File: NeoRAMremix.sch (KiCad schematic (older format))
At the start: 16 parts, among them P1 C64-Exp-Port, Q1 2N3904, U1 HM628512BFP-5, U2 HM628512BFP-5, U3 HM628512BFP-5, U4 HM628512BFP-5

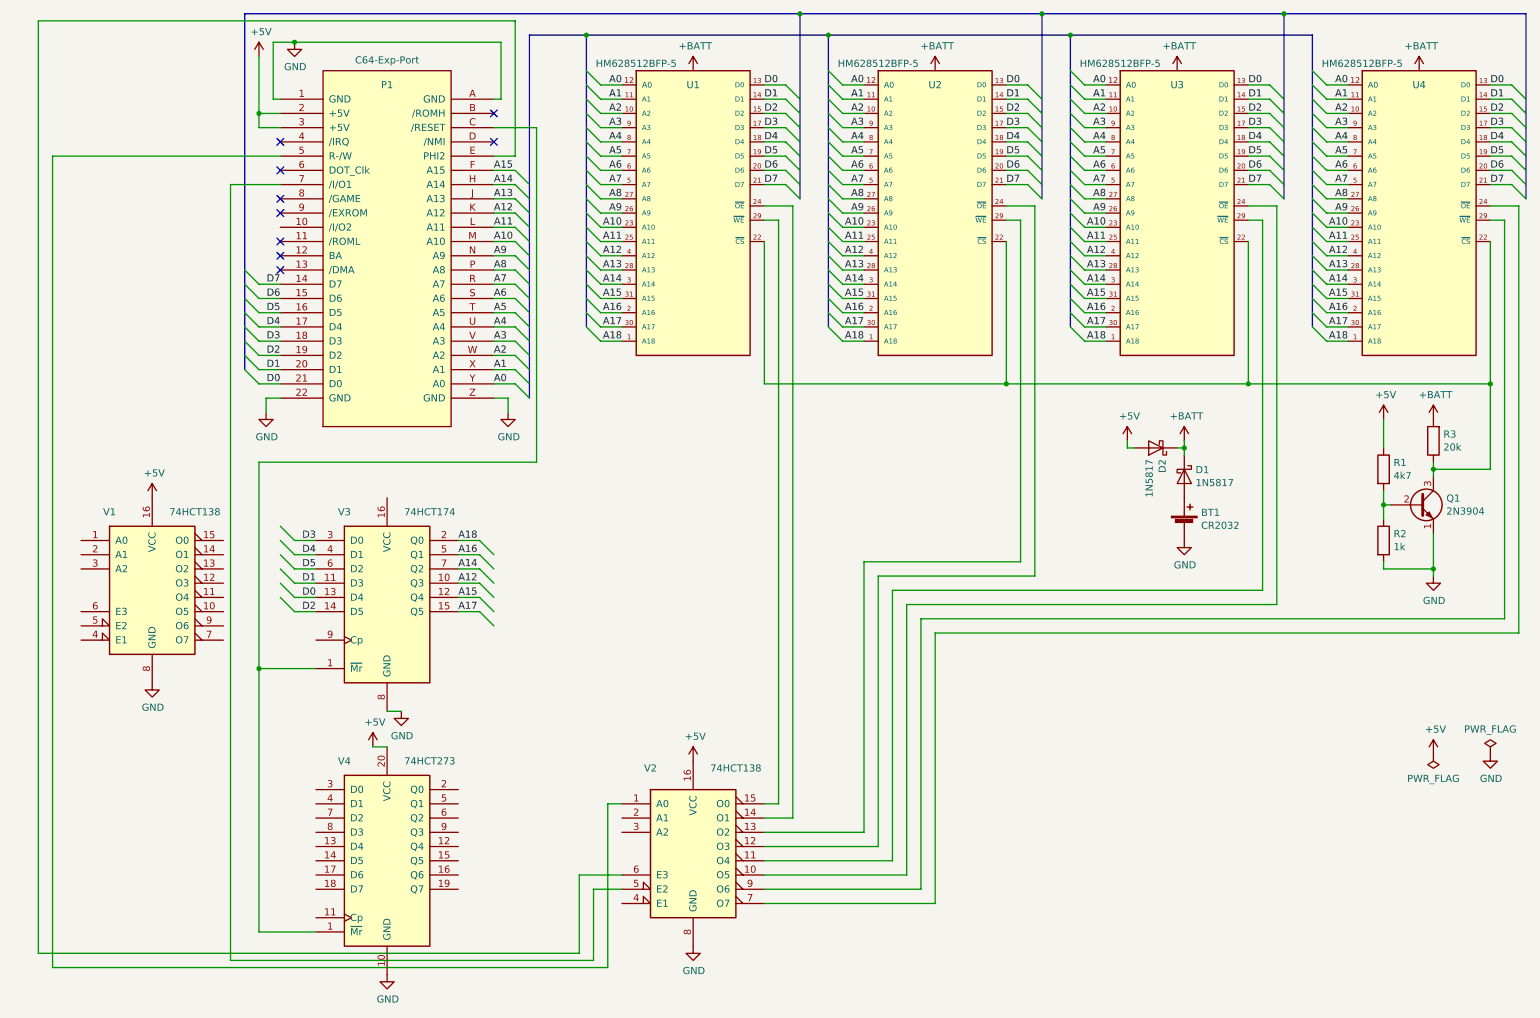
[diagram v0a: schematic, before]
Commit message: Completed and fixed schematics.
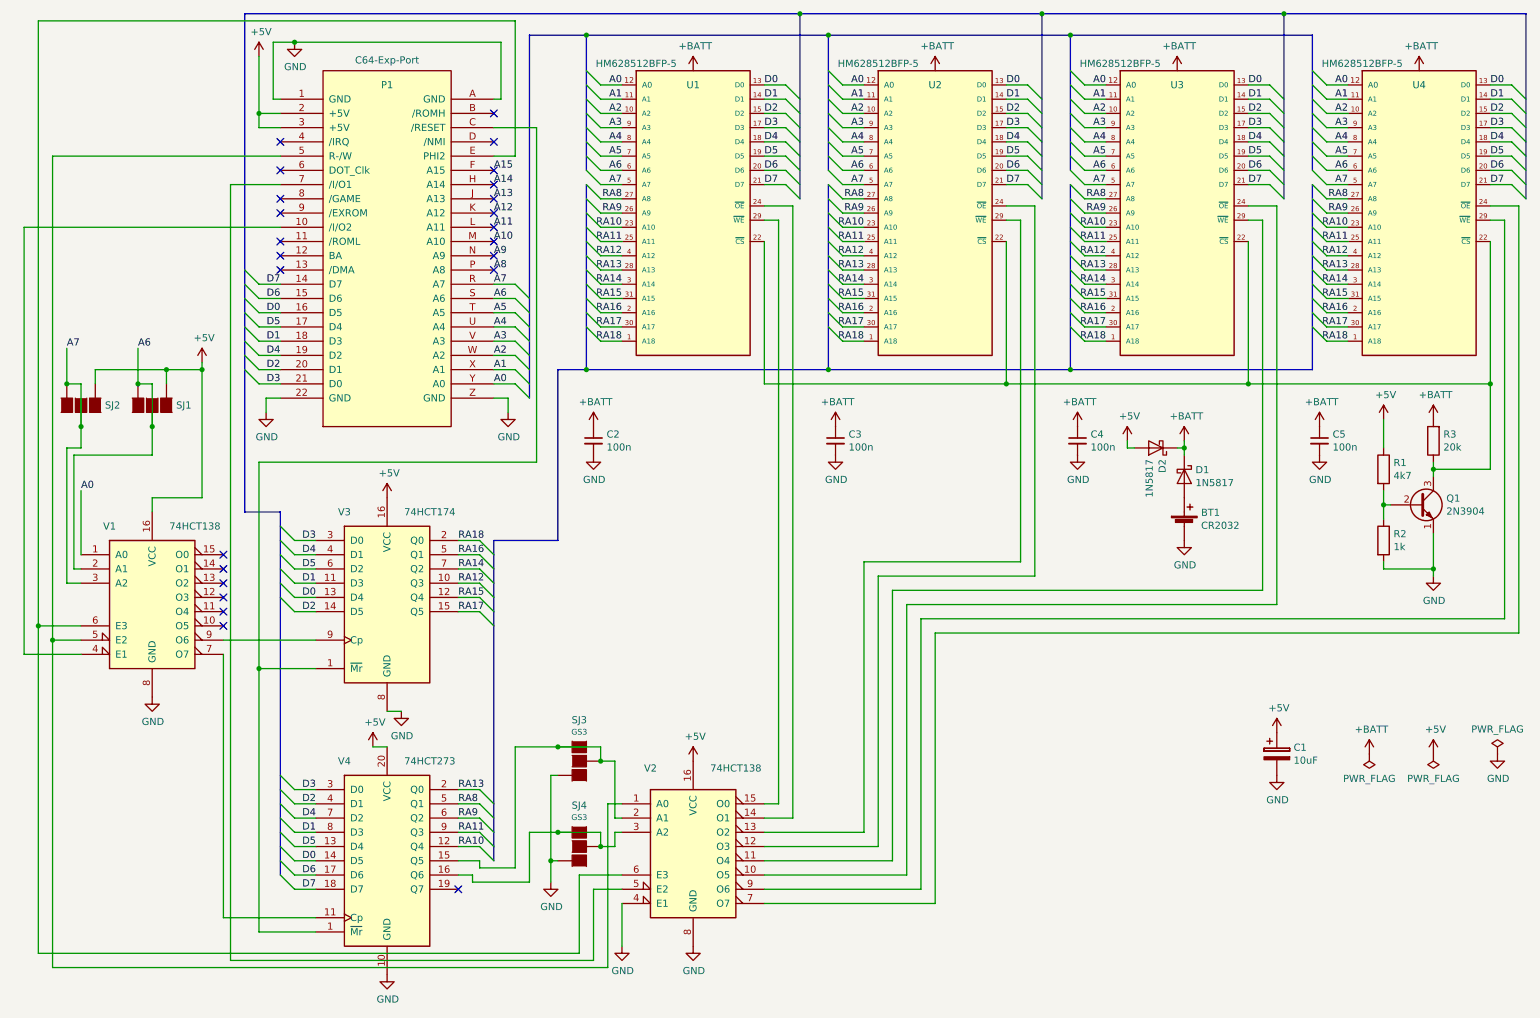
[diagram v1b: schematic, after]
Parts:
- added C1: 10uF, symbol device:CP
- added C2, C3, C4, C5: 100n, symbol device:C_Small
- added SJ1, SJ2, SJ3, SJ4: GS3, symbol NeoRAMremix-rescue:GS3-w_conn
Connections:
- net +5V: now also V3.16 (VCC), C1.1, SJ1.1 (G1), SJ2.1 (G1)
- net +BATT: now also C2.1, C3.1, C4.1, C5.1
- net A0: now also V1.1 (A0)
- net A10: no longer U1.23 (A10), U2.23 (A10), U3.23 (A10), U4.23 (A10)
- net A11: no longer U1.25 (A11), U2.25 (A11), U3.25 (A11), U4.25 (A11)
- net A12: no longer U1.4 (A12), U2.4 (A12), U3.4 (A12), U4.4 (A12), V3.10 (Q3)
- net A13: no longer U1.28 (A13), U2.28 (A13), U3.28 (A13), U4.28 (A13)
- net A14: no longer U1.3 (A14), U2.3 (A14), U3.3 (A14), U4.3 (A14), V3.7 (Q2)
- net A15: no longer U1.31 (A15), U2.31 (A15), U3.31 (A15), U4.31 (A15), V3.12 (Q4)
- net A6: now also V1.2 (A1), SJ1.2 (G2), SJ1.3 (G3)
- net A7: now also V1.3 (A2), SJ2.2 (G2), SJ2.3 (G3)
- net A8: no longer U1.27 (A8), U2.27 (A8), U3.27 (A8), U4.27 (A8)
- net A9: no longer U1.26 (A9), U2.26 (A9), U3.26 (A9), U4.26 (A9)
- net D0: now also P1.16 (D5), V4.14 (D5); no longer P1.21 (D0)
- net D1: now also P1.18 (D3), V4.8 (D3); no longer P1.20 (D1)
- net D2: now also P1.20 (D1), V4.4 (D1); no longer P1.19 (D2)
- net D3: now also P1.21 (D0), V4.3 (D0); no longer P1.18 (D3)
- net D4: now also P1.19 (D2), V4.7 (D2); no longer P1.17 (D4)
- net D5: now also P1.17 (D4), V4.13 (D4); no longer P1.16 (D5)
- net D6: now also V4.17 (D6)
- net D7: now also V4.18 (D7)
- net GND: now also V2.4 (E1), C1.2, C2.2, C3.2, C4.2, C5.2, SJ3.3 (G3), SJ4.3 (G3)
- net at P1.10 (/I/O2): now also V1.4 (E1)
- net at P1.5 (R-/W), V2.1 (A0): now also V1.5 (E2)
- net at P1.E (PHI2), V2.6 (E3): now also V1.6 (E3)
- net at V1.7 (O7): now also V4.11 (Cp)
- net at V1.9 (O6): now also V3.9 (Cp)
- net RA10: now reaches V4.12 (Q4)
- net RA10: now also U1.23 (A10), U2.23 (A10), U3.23 (A10), U4.23 (A10)
- net at V4.15 (Q5): now also V2.2 (A1), SJ3.1 (G1), SJ3.2 (G2)
- net at V4.16 (Q6): now also V2.3 (A2), SJ4.1 (G1), SJ4.2 (G2)
- net RA13: now reaches V4.2 (Q0)
- net RA13: now also U1.28 (A13), U2.28 (A13), U3.28 (A13), U4.28 (A13)
- net RA8: now reaches V4.5 (Q1)
- net RA8: now also U1.27 (A8), U2.27 (A8), U3.27 (A8), U4.27 (A8)
- net RA9: now reaches V4.6 (Q2)
- net RA9: now also U1.26 (A9), U2.26 (A9), U3.26 (A9), U4.26 (A9)
- net RA11: now reaches V4.9 (Q3)
- net RA11: now also U1.25 (A11), U2.25 (A11), U3.25 (A11), U4.25 (A11)
- net A16 renamed RA16
- net A17 renamed RA17
- net A18 renamed RA18
- new net RA12: U1.4 (A12), U2.4 (A12), U3.4 (A12), U4.4 (A12), V3.10 (Q3)
- new net RA14: U1.3 (A14), U2.3 (A14), U3.3 (A14), U4.3 (A14), V3.7 (Q2)
- new net RA15: U1.31 (A15), U2.31 (A15), U3.31 (A15), U4.31 (A15), V3.12 (Q4)
- no-connect marks 9 -> 24
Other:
- moved on the sheet: V1

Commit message: Started layout.
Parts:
- added H1: MountingHole, Mounting_Holes:MountingHole_5mm, symbol Mechanical:MountingHole
- BT1: footprint (none) -> hackup:Battery-Holder-CR2032
- C1: footprint (none) -> Capacitors_THT:CP_Radial_D5.0mm_P2.00mm
- C2, C3, C4, C5: footprint (none) -> Capacitors_THT:C_Disc_D4.3mm_W1.9mm_P5.00mm
- D1, D2: footprint Diode_THT:D_DO-41_SOD81_P10.16mm_Horizontal -> Diodes_THT:D_DO-41_SOD81_P5.08mm_Vertical_KathodeUp
- R1, R2, R3: footprint (none) -> Resistors_THT:R_Axial_DIN0207_L6.3mm_D2.5mm_P2.54mm_Vertical
- SJ1, SJ2, SJ3, SJ4: footprint (none) -> Connectors:GS3
- V1, V2, V3: footprint Housings_DIP:DIP-16_W7.62mm_LongPads -> Housings_DIP:DIP-16_W7.62mm
- V4: footprint Housings_DIP:DIP-20_W7.62mm_LongPads -> Housings_DIP:DIP-20_W7.62mm
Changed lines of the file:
@@
 F 0 "V1" H 1100 5400 50  0000 C CNN
 F 1 "74HCT138" H 1700 5400 50  0000 C CNN
-F 2 "Housings_DIP:DIP-16_W7.62mm_LongPads" H 1400 4900 50  0001 C CNN
+F 2 "Housings_DIP:DIP-16_W7.62mm" H 1400 4900 50  0001 C CNN
 F 3 "http://www.ti.com/lit/gpn/sn74LS138" H 1400 4900 50  0001 C CNN
 	1    1400 4900
@@
 F 0 "V3" H 2750 5500 50  0000 C CNN
 F 1 "74HCT174" H 3350 5500 50  0000 C CNN
-F 2 "Housings_DIP:DIP-16_W7.62mm_LongPads" H 3050 4900 50  0001 C CNN
+F 2 "Housings_DIP:DIP-16_W7.62mm" H 3050 4900 50  0001 C CNN
 F 3 "http://www.ti.com/lit/gpn/sn74LS174" H 3050 4900 50  0001 C CNN
 	1    3050 4900
@@
 F 0 "V4" H 2750 7450 50  0000 C CNN
 F 1 "74HCT273" H 3350 7450 50  0000 C CNN
-F 2 "Housings_DIP:DIP-20_W7.62mm_LongPads" H 3050 6750 50  0001 C CNN
+F 2 "Housings_DIP:DIP-20_W7.62mm" H 3050 6750 50  0001 C CNN
 F 3 "http://www.ti.com/lit/gpn/sn74LS273" H 3050 6750 50  0001 C CNN
 	1    3050 6750
@@
 F 0 "V2" H 4900 7200 50  0000 C CNN
 F 1 "74HCT138" H 5500 7200 50  0000 C CNN
-F 2 "Housings_DIP:DIP-16_W7.62mm_LongPads" H 5200 6650 50  0001 C CNN
+F 2 "Housings_DIP:DIP-16_W7.62mm" H 5200 6650 50  0001 C CNN
 F 3 "http://www.ti.com/lit/gpn/sn74LS138" H 5200 6650 50  0001 C CNN
 	1    5200 6650
@@
 F 0 "BT1" H 8768 4496 50  0000 L CNN
 F 1 "CR2032" H 8768 4405 50  0000 L CNN
-F 2 "" V 8650 4460 50  0001 C CNN
+F 2 "hackup:Battery-Holder-CR2032" V 8650 4460 50  0001 C CNN
 F 3 "~" V 8650 4460 50  0001 C CNN
 	1    8650 4400
@@
 F 0 "D1" V 8604 4129 50  0000 L CNN
 F 1 "1N5817" V 8695 4129 50  0000 L CNN
-F 2 "Diode_THT:D_DO-41_SOD81_P10.16mm_Horizontal" H 8650 3875 50  0001 C CNN
+F 2 "Diodes_THT:D_DO-41_SOD81_P5.08mm_Vertical_KathodeUp" H 8650 3875 50  0001 C CNN
 F 3 "http://www.vishay.com/docs/88525/1n5817.pdf" H 8650 4050 50  0001 C CNN
 	1    8650 4050
@@
 F 0 "R3" H 10330 3754 50  0000 R CNN
 F 1 "20k" H 10330 3845 50  0000 R CNN
-F 2 "" V 10330 3800 50  0001 C CNN
+F 2 "Resistors_THT:R_Axial_DIN0207_L6.3mm_D2.5mm_P2.54mm_Vertical" V 10330 3800 50  0001 C CNN
 F 3 "~" H 10400 3800 50  0001 C CNN
 	1    10400 3800
@@
 F 0 "R1" H 10120 4046 50  0000 L CNN
 F 1 "4k7" H 10120 3955 50  0000 L CNN
-F 2 "" V 9980 4000 50  0001 C CNN
+F 2 "Resistors_THT:R_Axial_DIN0207_L6.3mm_D2.5mm_P2.54mm_Vertical" V 9980 4000 50  0001 C CNN
 F 3 "~" H 10050 4000 50  0001 C CNN
 	1    10050 4000
@@
 F 0 "R2" H 10120 4546 50  0000 L CNN
 F 1 "1k" H 10120 4455 50  0000 L CNN
-F 2 "" V 9980 4500 50  0001 C CNN
+F 2 "Resistors_THT:R_Axial_DIN0207_L6.3mm_D2.5mm_P2.54mm_Vertical" V 9980 4500 50  0001 C CNN
 F 3 "~" H 10050 4500 50  0001 C CNN
 	1    10050 4500
@@
 F 0 "D2" V 8404 3929 50  0000 L CNN
 F 1 "1N5817" V 8495 3929 50  0000 L CNN
-F 2 "Diode_THT:D_DO-41_SOD81_P10.16mm_Horizontal" H 8450 3675 50  0001 C CNN
+F 2 "Diodes_THT:D_DO-41_SOD81_P5.08mm_Vertical_KathodeUp" H 8450 3675 50  0001 C CNN
 F 3 "http://www.vishay.com/docs/88525/1n5817.pdf" H 8450 3850 50  0001 C CNN
 	1    8450 3850
@@
 F 0 "C2" H 4592 3846 50  0000 L CNN
 F 1 "100n" H 4592 3755 50  0000 L CNN
-F 2 "" H 4500 3800 50  0001 C CNN
+F 2 "Capacitors_THT:C_Disc_D4.3mm_W1.9mm_P5.00mm" H 4500 3800 50  0001 C CNN
 F 3 "~" H 4500 3800 50  0001 C CNN
 	1    4500 3800
@@
 F 0 "C3" H 6292 3846 50  0000 L CNN
 F 1 "100n" H 6292 3755 50  0000 L CNN
-F 2 "" H 6200 3800 50  0001 C CNN
+F 2 "Capacitors_THT:C_Disc_D4.3mm_W1.9mm_P5.00mm" H 6200 3800 50  0001 C CNN
 F 3 "~" H 6200 3800 50  0001 C CNN
 	1    6200 3800
@@
 F 0 "C4" H 7992 3846 50  0000 L CNN
 F 1 "100n" H 7992 3755 50  0000 L CNN
-F 2 "" H 7900 3800 50  0001 C CNN
+F 2 "Capacitors_THT:C_Disc_D4.3mm_W1.9mm_P5.00mm" H 7900 3800 50  0001 C CNN
 F 3 "~" H 7900 3800 50  0001 C CNN
 	1    7900 3800
@@
 F 0 "C5" H 9692 3846 50  0000 L CNN
 F 1 "100n" H 9692 3755 50  0000 L CNN
-F 2 "" H 9600 3800 50  0001 C CNN
+F 2 "Capacitors_THT:C_Disc_D4.3mm_W1.9mm_P5.00mm" H 9600 3800 50  0001 C CNN
 F 3 "~" H 9600 3800 50  0001 C CNN
 	1    9600 3800
@@
 F 0 "SJ3" H 4400 6339 50  0000 C CNN
 F 1 "GS3" H 4400 6255 40  0000 C CNN
-F 2 "" H 4400 6050 50  0001 C CNN
+F 2 "Connectors:GS3" H 4400 6050 50  0001 C CNN
 F 3 "" H 4400 6050 50  0001 C CNN
 	1    4400 6050
@@
 F 0 "SJ4" H 4400 6939 50  0000 C CNN
 F 1 "GS3" H 4400 6855 40  0000 C CNN
-F 2 "" H 4400 6650 50  0001 C CNN
+F 2 "Connectors:GS3" H 4400 6650 50  0001 C CNN
 F 3 "" H 4400 6650 50  0001 C CNN
 	1    4400 6650
@@
 F 0 "SJ1" V 1400 3718 50  0000 L CNN
 F 1 "GS3" V 1446 3718 40  0001 L CNN
-F 2 "" H 1400 3550 50  0001 C CNN
+F 2 "Connectors:GS3" H 1400 3550 50  0001 C CNN
 F 3 "" H 1400 3550 50  0001 C CNN
 	1    1400 3550
@@
 F 0 "SJ2" V 900 3718 50  0000 L CNN
 F 1 "GS3" V 946 3718 40  0001 L CNN
-F 2 "" H 900 3550 50  0001 C CNN
+F 2 "Connectors:GS3" H 900 3550 50  0001 C CNN
 F 3 "" H 900 3550 50  0001 C CNN
 	1    900  3550
@@
 F 0 "C1" H 9418 6046 50  0000 L CNN
 F 1 "10uF" H 9418 5955 50  0000 L CNN
-F 2 "" H 9338 5850 50  0001 C CNN
+F 2 "Capacitors_THT:CP_Radial_D5.0mm_P2.00mm" H 9338 5850 50  0001 C CNN
 F 3 "~" H 9300 6000 50  0001 C CNN
 	1    9300 6000
@@
 NoConn ~ 3800 2500
 NoConn ~ 3800 2600
+$Comp
+L Mechanical:MountingHole H1
+U 1 1 5C38DAA3
+P 7250 6300
+F 0 "H1" H 7350 6346 50  0000 L CNN
+F 1 "MountingHole" H 7350 6255 50  0000 L CNN
+F 2 "Mounting_Holes:MountingHole_5mm" H 7250 6300 50  0001 C CNN
+F 3 "~" H 7250 6300 50  0001 C CNN
+	1    7250 6300
+	1    0    0    -1
+$EndComp
 Wire Bus Line
 	6150 2000 6150 3300

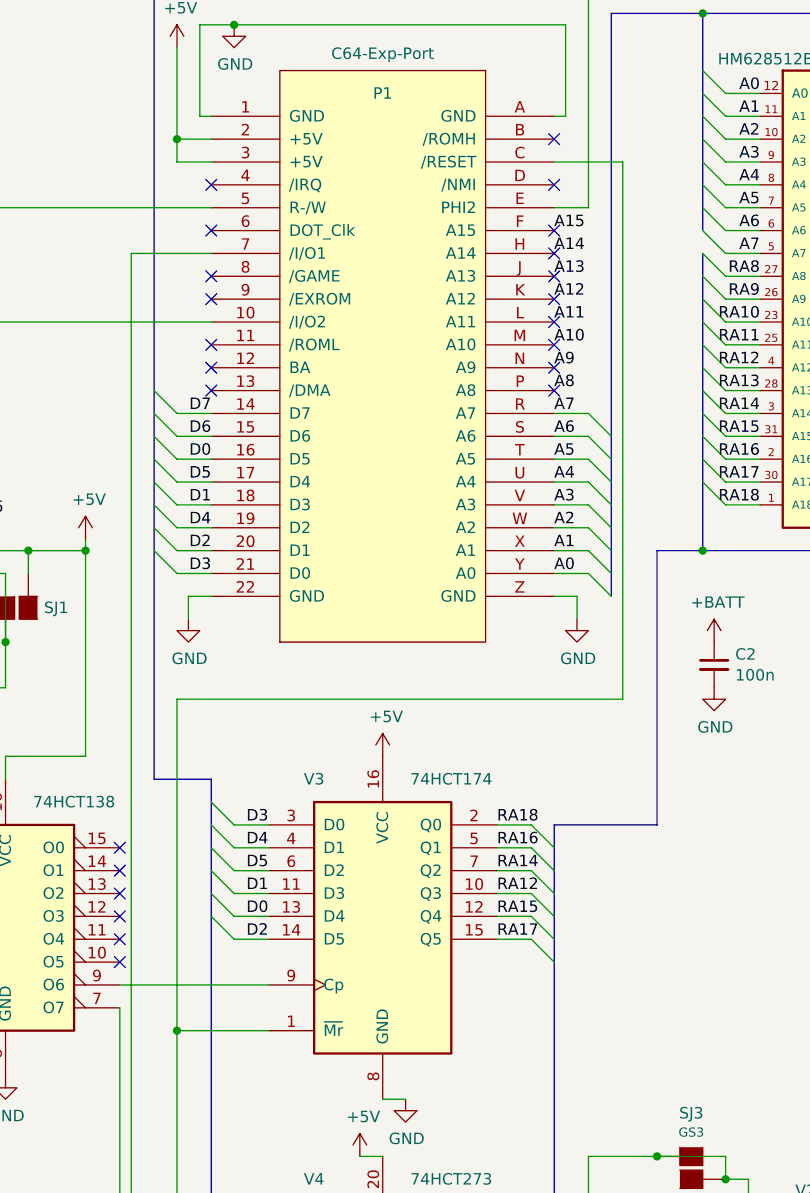
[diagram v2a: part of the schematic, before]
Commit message: Reset switch.
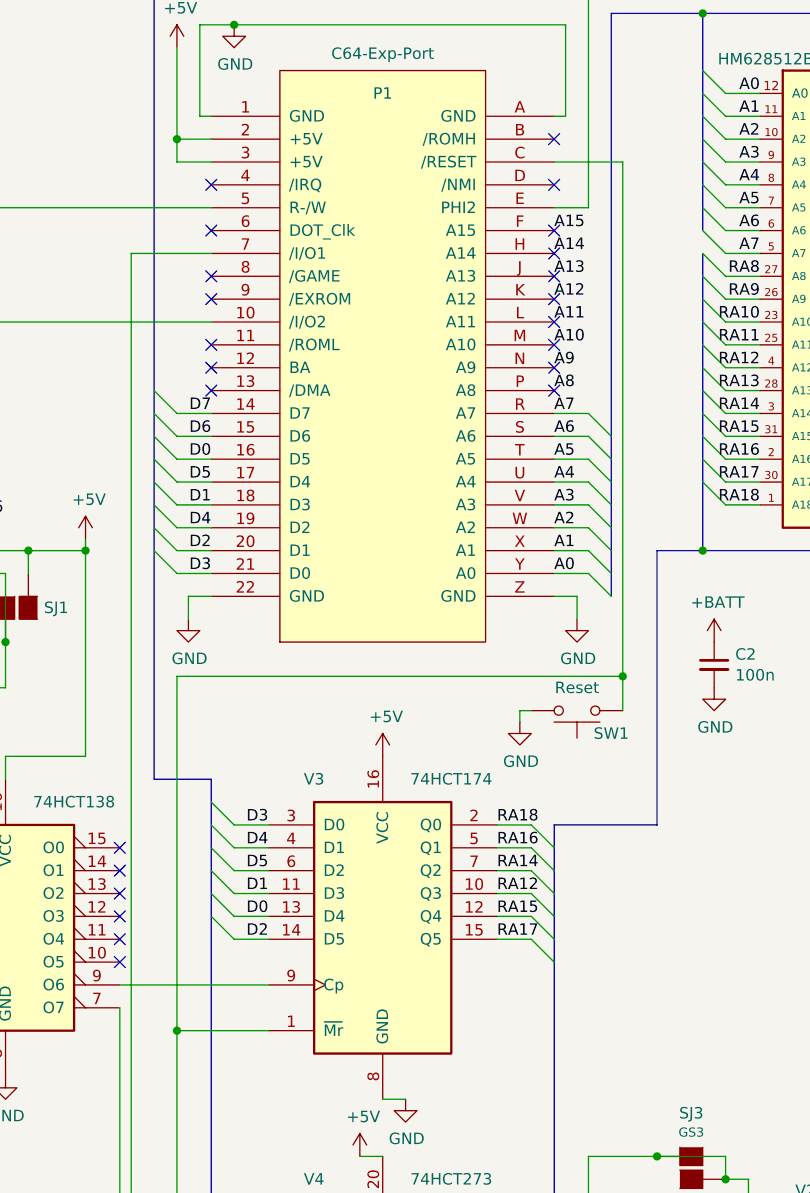
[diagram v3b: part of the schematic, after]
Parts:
- added SW1: Reset, Buttons_Switches_THT:SW_Tactile_SPST_Angled_PTS645Vx83-2LFS, symbol Switch:SW_Push
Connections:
- net GND: now also SW1.2
- net at P1.C (/RESET), V3.1 (~Mr), V4.1 (~Mr): now also SW1.1
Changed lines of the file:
@@
 encoding utf-8
 Sheet 1 1
-Title ""
+Title "NeoRAM Remix"
 Date ""
-Rev ""
-Comp ""
-Comment1 ""
-Comment2 ""
+Rev "1"
+Comp "hackup.net"
+Comment1 "Based on NeoRAM by N. Welte (2007) http://www.1541.de"
+Comment2 "For non-profit and personal use only!"
 Comment3 ""
 Comment4 ""
@@
 	3800 1600 4100 1600
 Wire Wire Line
-	4100 1600 4100 3950
-Wire Wire Line
-	4100 3950 2150 3950
-Wire Wire Line
-	2150 3950 2150 5400
+	4100 1600 4100 3850
+Wire Wire Line
+	4100 3850 2150 3850
+Wire Wire Line
+	2150 3850 2150 5400
 Wire Wire Line
 	2150 5400 2550 5400
@@
 	1    0    0    -1
 $EndComp
+$Comp
+L Switch:SW_Push SW1
+U 1 1 5C47CB67
+P 3900 4000
+F 0 "SW1" H 3750 4100 50  0000 C CNN
+F 1 "Reset" H 3900 3900 50  0000 C CNN
+F 2 "Buttons_Switches_THT:SW_Tactile_SPST_Angled_PTS645Vx83-2LFS" H 3900 4200 50  0001 C CNN
+F 3 "" H 3900 4200 50  0001 C CNN
+	1    3900 4000
+	-1   0    0    1
+$EndComp
+Wire Wire Line
+	4100 4000 4100 3850
+Connection ~ 4100 3850
+$Comp
+L power:GND #PWR0138
+U 1 1 5C4A1311
+P 3650 4050
+F 0 "#PWR0138" H 3650 3800 50  0001 C CNN
+F 1 "GND" H 3655 3877 50  0000 C CNN
+F 2 "" H 3650 4050 50  0001 C CNN
+F 3 "" H 3650 4050 50  0001 C CNN
+	1    3650 4050
+	1    0    0    -1
+$EndComp
+Wire Wire Line
+	3650 4050 3650 4000
+Wire Wire Line
+	3650 4000 3700 4000
 Wire Bus Line
 	6150 2000 6150 3300
